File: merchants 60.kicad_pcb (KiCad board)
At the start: 4 copper layers, 304.8 x 122.2 mm, 182 parts, among them SW1 SW_PUSH, U1 ATmega32U4-AU, Y1 16MHz

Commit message: Converting the PCB from 4 layer to 2 layer
Im fucking retarded but I'm also a fucking god
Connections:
- U1 pad 27: row5 -> row3
- U1 pad 29: row3 -> row5
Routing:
- net col10: track 288.2 -> 350.9 mm, vias 1 -> 5
- net col11: track 319.4 -> 371.3 mm, vias 1 -> 7
- net col0: track 163.3 -> 120.7 mm, vias 1 -> 0
- net VCC: track 150.8 -> 185.5 mm, vias 2 -> 3
- net row2: track 314.6 -> 348.0 mm, vias 1 -> 2
- net col8: track 231.5 -> 260.1 mm, vias 1 -> 3
- net col15: track 459.2 -> 431.2 mm, vias 1 -> 3
- net col7: track 211.6 -> 238.8 mm, vias 1 -> 6
- net GND: track 282.8 -> 307.0 mm
- net col12: track 343.8 -> 366.8 mm, vias 1 -> 3
- net D+: track 160.2 -> 182.1 mm, vias 2 -> 1
- net col14: track 424.8 -> 403.1 mm, vias 1 -> 3
- net D-: track 159.1 -> 179.8 mm, vias 2 -> 1
- net row1: track 317.6 -> 335.3 mm, vias 1 -> 2
- net col9: track 281.0 -> 296.6 mm, vias 1 -> 3
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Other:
- board size 304.8 x 122.2 mm -> 304.8 x 123.8 mm
- copper layers 4 -> 2

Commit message: Minor Changes
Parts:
- USB1: moved to B.Cu
- turned USB1 to 0 degrees
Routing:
- net GND: track 307.0 -> 286.5 mm, vias 2 -> 3
- net D+: track 182.1 -> 177.5 mm, vias 1 -> 2
- net D-: track 179.8 -> 176.3 mm, vias 1 -> 2
- net VCC: track 185.5 -> 184.5 mm, vias 3 -> 4

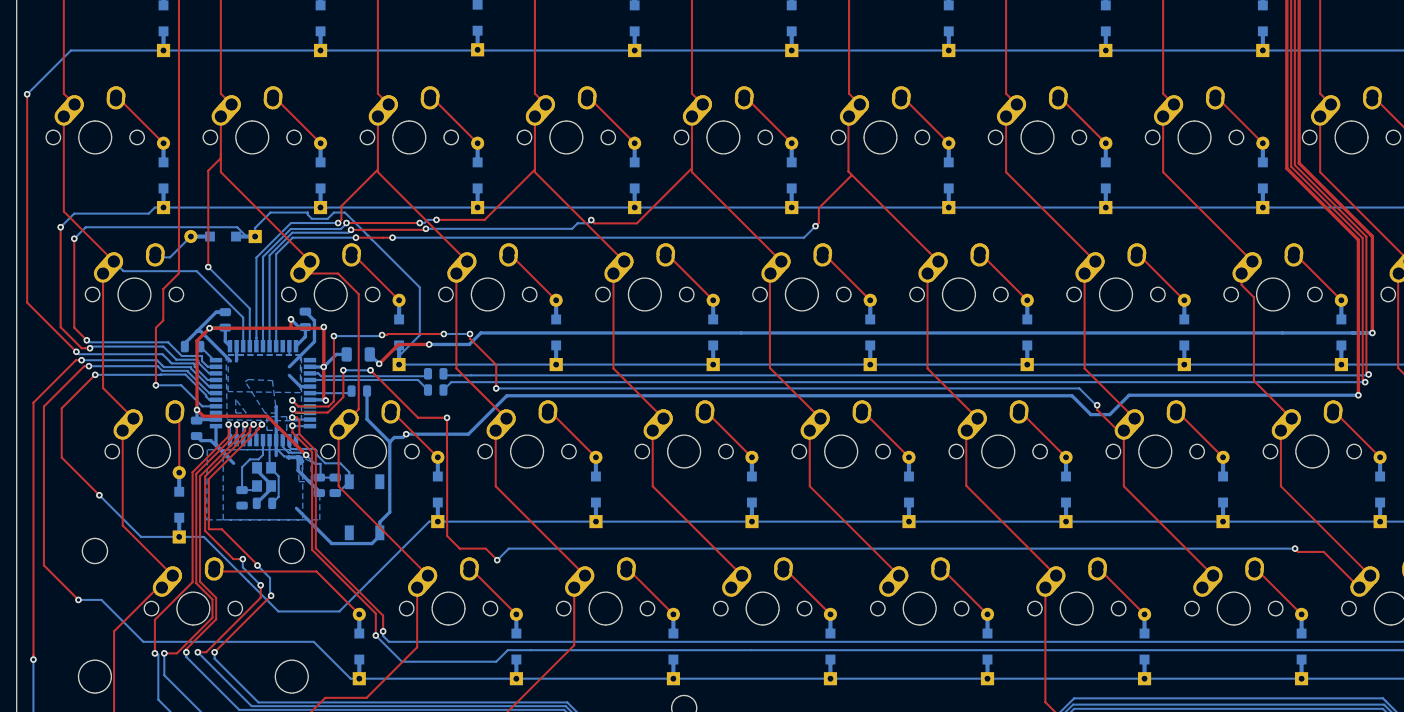
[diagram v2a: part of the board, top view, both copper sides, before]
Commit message: slight routing changes
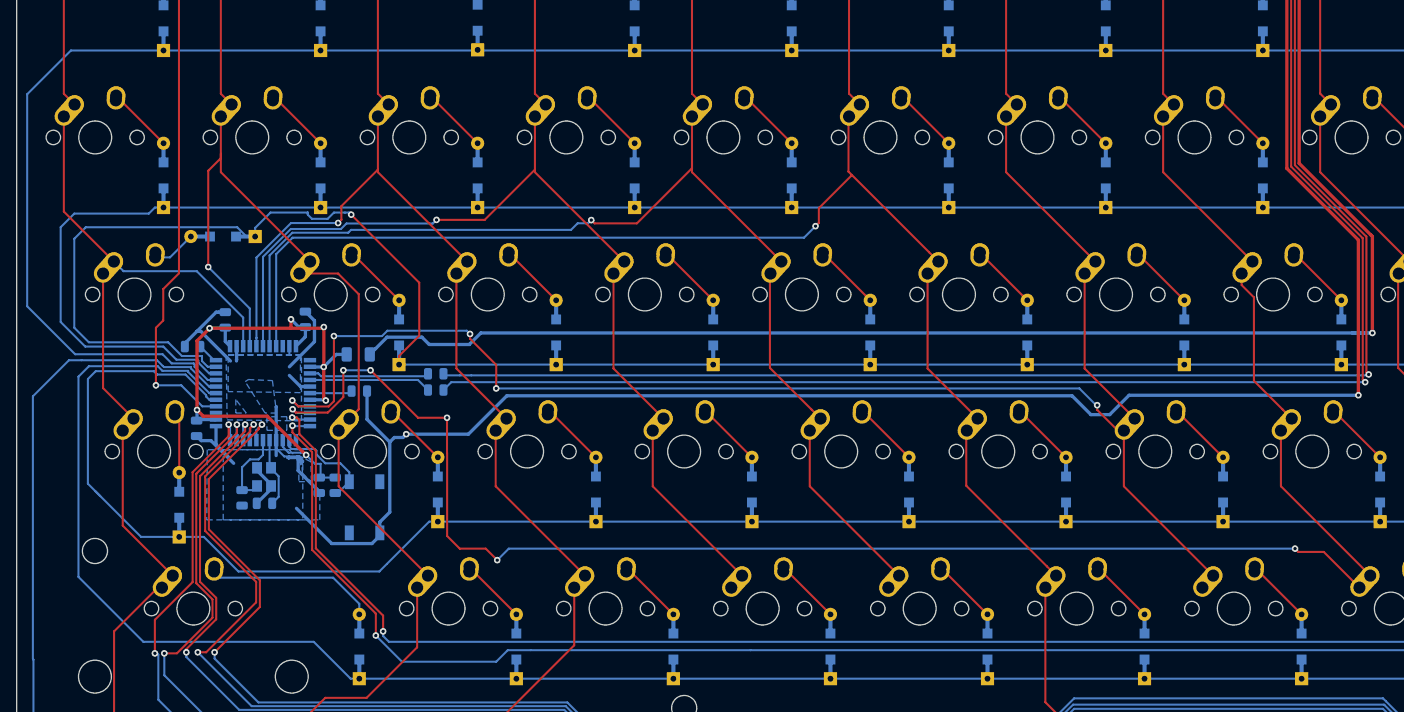
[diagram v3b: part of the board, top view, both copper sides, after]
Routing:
- net row3: track 343.0 -> 337.5 mm, vias 2 -> 0
- net row4: track 349.6 -> 344.1 mm, vias 2 -> 0
- net col10: track 350.9 -> 348.9 mm, vias 5 -> 3
- net col11: track 371.3 -> 370.1 mm, vias 7 -> 5
- net Net-(D5-Pad2): track 19.8 -> 20.5 mm
- net row5: track 368.2 -> 368.8 mm, vias 2 -> 0
- net row1: track 335.3 -> 334.7 mm, vias 2 -> 0
- net row2: track 348.0 -> 348.5 mm, vias 2 -> 1
- net col6: track 201.5 -> 201.8 mm, vias 7 -> 5
- net row0: track 356.7 -> 357.0 mm, vias 2 -> 0
- net VCC: track 184.5 -> 184.3 mm, vias 4 -> 2
- net col3: vias 3 -> 1
- net col5: vias 3 -> 1
- net col4: vias 3 -> 1

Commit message: Rerouting traces
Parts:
- moved SW1 36.1 mm to (74.7, 132.0), turned to 180 degrees
- moved R2 27.8 mm to (89.2, 148.0), turned to 270 degrees
- moved R1 27.0 mm to (91.1, 148.0), turned to 270 degrees
- moved R3 26.5 mm to (82.0, 130.4)
- moved C4 25.8 mm to (87.3, 123.7), turned to 180 degrees
- moved C5 24.3 mm to (84.6, 127.4), turned to 270 degrees
- moved Y1 20.7 mm to (87.3, 127.0), turned to 270 degrees
- moved F1 20.4 mm to (93.2, 148.6), turned to 90 degrees
- moved R4 20.2 mm to (104.9, 132.8), turned to 180 degrees
- moved C7 19.3 mm to (87.5, 144.4), turned to 270 degrees
- moved C6 14.9 mm to (84.5, 132.5)
- moved C1 11.9 mm to (95.9, 146.3), turned to 90 degrees
- moved C3 11.7 mm to (103.9, 136.7)
- moved C2 5.62 mm to (93.9, 125.2), turned to 270 degrees
- moved D15 5.40 mm to (128.9, 123.8)
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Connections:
- U1 pad 10: col8 -> row5
- U1 pad 11: col9 -> row0
- U1 pad 18: col10 -> row1
- U1 pad 19: col11 -> col0
- U1 pad 20: col12 -> col1
- U1 pad 21: col13 -> col2
- U1 pad 22: col14 -> row2
- U1 pad 27: row3 -> col14
- U1 pad 28: row4 -> col13
- U1 pad 29: row5 -> col12
- U1 pad 30: row0 -> col11
- U1 pad 31: row1 -> col10
- U1 pad 32: row2 -> col9
- U1 pad 36: col0 -> col8
- U1 pad 37: col1 -> col7
- U1 pad 38: col2 -> col6
- U1 pad 39: col3 -> col5
- U1 pad 41: col5 -> col3
- U1 pad 8: col6 -> row3
- U1 pad 9: col7 -> row4
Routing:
- net D+: track 177.5 -> 306.3 mm, vias 2 -> 6
- net D-: track 176.3 -> 304.1 mm, vias 2 -> 6
- net col11: track 370.1 -> 251.6 mm, vias 5 -> 1
- net VCC: track 184.3 -> 301.3 mm, vias 2 -> 6
- net col10: track 348.9 -> 254.4 mm, vias 3 -> 1
- net GND: track 286.5 -> 379.7 mm, vias 3 -> 8
- net col15: track 431.2 -> 350.7 mm, vias 3 -> 1
- net col14: track 403.1 -> 335.5 mm, vias 3 -> 1
- net col12: track 366.8 -> 313.9 mm, vias 3 -> 1
- net col13: track 390.2 -> 337.7 mm, vias 3 -> 1
- net row2: track 348.5 -> 303.2 mm, vias 1 -> 4
- net col9: track 296.6 -> 254.3 mm, vias 3 -> 1
- net row3: track 337.5 -> 305.8 mm
- net row1: track 334.7 -> 312.1 mm, vias 0 -> 1
- net col8: track 260.1 -> 239.3 mm
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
